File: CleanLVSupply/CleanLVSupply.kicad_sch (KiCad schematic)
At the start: 7 parts, among them J1 12VIN, J2 5V, J3 5V, J4 5V, J5 +-15V, J6 +-15V

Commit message: CleanLVSupply fixes, HiFiDAC skeleton
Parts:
- J5, J6: footprint BW_Connectors:Amphenol_MINITEK_0.8_3P_V -> BW_Connectors:Amphenol_MINITEK_0.8_4P_V; symbol Connector:Conn_01x03_Pin -> Connector:Conn_01x04_Pin
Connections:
- net -15V: now also J5.4 (Pin_4), J6.4 (Pin_4); no longer J5.3 (Pin_3), J6.3 (Pin_3)
- net GND: now also J5.3 (Pin_3), J6.3 (Pin_3)
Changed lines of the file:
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@@
-	)
-	(junction
-		(at 146.05 106.68)
-		(diameter 0)
-		(color 0 0 0 0)
 	)
 	(junction
@@
 	)
 	(junction
+		(at 146.05 109.22)
+		(diameter 0)
+		(color 0 0 0 0)
+	)
+	(junction
+		(at 173.99 90.17)
+		(diameter 0)
+		(color 0 0 0 0)
+	)
+	(junction
 		(at 59.69 110.49)
 		(diameter 0)
@@
 		(color 0 0 0 0)
 	)
+	(junction
+		(at 173.99 104.14)
+		(diameter 0)
+		(color 0 0 0 0)
+	)
 	(wire
 		(pts
@@
 	(wire
 		(pts
-			(xy 176.53 92.71) (xy 146.05 92.71)
-		)
-		(stroke
-			(width 0)
-			(type default)
-		)
-	)
-	(wire
-		(pts
 			(xy 59.69 88.9) (xy 104.14 88.9)
 		)
@@
 	(wire
 		(pts
+			(xy 146.05 109.22) (xy 146.05 95.25)
+		)
+		(stroke
+			(width 0)
+			(type default)
+		)
+	)
+	(wire
+		(pts
 			(xy 87.63 83.82) (xy 87.63 46.99)
 		)
@@
 	(wire
 		(pts
-			(xy 146.05 106.68) (xy 146.05 110.49)
+			(xy 176.53 106.68) (xy 173.99 106.68)
 		)
 		(stroke
@@
 	(wire
 		(pts
+			(xy 173.99 90.17) (xy 176.53 90.17)
+		)
+		(stroke
+			(width 0)
+			(type default)
+		)
+	)
+	(wire
+		(pts
 			(xy 87.63 34.29) (xy 87.63 36.83)
 		)
@@
 	(wire
 		(pts
+			(xy 173.99 104.14) (xy 156.21 104.14)
+		)
+		(stroke
+			(width 0)
+			(type default)
+		)
+	)
+	(wire
+		(pts
 			(xy 68.58 48.26) (xy 68.58 52.07)
 		)
@@
 	(wire
 		(pts
-			(xy 156.21 90.17) (xy 176.53 90.17)
+			(xy 156.21 90.17) (xy 173.99 90.17)
 		)
 		(stroke
@@
 	(wire
 		(pts
+			(xy 146.05 95.25) (xy 176.53 95.25)
+		)
+		(stroke
+			(width 0)
+			(type default)
+		)
+	)
+	(wire
+		(pts
 			(xy 59.69 68.58) (xy 59.69 88.9)
 		)
@@
 	(wire
 		(pts
+			(xy 173.99 92.71) (xy 173.99 90.17)
+		)
+		(stroke
+			(width 0)
+			(type default)
+		)
+	)
+	(wire
+		(pts
 			(xy 166.37 87.63) (xy 176.53 87.63)
 		)
@@
 	(wire
 		(pts
-			(xy 176.53 106.68) (xy 146.05 106.68)
+			(xy 146.05 110.49) (xy 146.05 109.22)
 		)
 		(stroke
@@
 	(wire
 		(pts
+			(xy 146.05 109.22) (xy 176.53 109.22)
+		)
+		(stroke
+			(width 0)
+			(type default)
+		)
+	)
+	(wire
+		(pts
 			(xy 166.37 41.91) (xy 176.53 41.91)
 		)
@@
 	(wire
 		(pts
+			(xy 173.99 106.68) (xy 173.99 104.14)
+		)
+		(stroke
+			(width 0)
+			(type default)
+		)
+	)
+	(wire
+		(pts
 			(xy 156.21 104.14) (xy 156.21 90.17)
 		)
@@
 	(wire
 		(pts
-			(xy 146.05 92.71) (xy 146.05 106.68)
-		)
-		(stroke
-			(width 0)
-			(type default)
-		)
-	)
-	(wire
-		(pts
-			(xy 176.53 104.14) (xy 156.21 104.14)
+			(xy 176.53 104.14) (xy 173.99 104.14)
 		)
 		(stroke
@@
 		(pts
 			(xy 104.14 105.41) (xy 87.63 105.41)
+		)
+		(stroke
+			(width 0)
+			(type default)
+		)
+	)
+	(wire
+		(pts
+			(xy 176.53 92.71) (xy 173.99 92.71)
 		)
 		(stroke
@@
 	)
 	(symbol
-		(lib_id "Connector:Conn_01x03_Pin")
+		(lib_id "Connector:Conn_01x04_Pin")
 		(at 181.61 104.14 0)
 		(mirror y)
@@
 			)
 		)
-		(property "Footprint" "BW_Connectors:Amphenol_MINITEK_0.8_3P_V"
+		(property "Footprint" "BW_Connectors:Amphenol_MINITEK_0.8_4P_V"
 			(at 181.61 104.14 0)
 			(effects
@@
 			)
 		)
-		(property "Description" "Generic connector, single row, 01x03, script generated"
+		(property "Description" "Generic connector, single row, 01x04, script generated"
 			(at 181.61 104.14 0)
 			(effects
@@
 		)
 		(pin "3"
+		)
+		(pin "4"
 		)
 		(instances
@@
 	)
 	(symbol
-		(lib_id "Connector:Conn_01x03_Pin")
+		(lib_id "Connector:Conn_01x04_Pin")
 		(at 181.61 90.17 0)
 		(mirror y)
@@
 			)
 		)
-		(property "Footprint" "BW_Connectors:Amphenol_MINITEK_0.8_3P_V"
+		(property "Footprint" "BW_Connectors:Amphenol_MINITEK_0.8_4P_V"
 			(at 181.61 90.17 0)
 			(effects
@@
 			)
 		)
-		(property "Description" "Generic connector, single row, 01x03, script generated"
+		(property "Description" "Generic connector, single row, 01x04, script generated"
 			(at 181.61 90.17 0)
 			(effects
@@
 		(pin "3"
 		)
+		(pin "4"
+		)
 		(instances

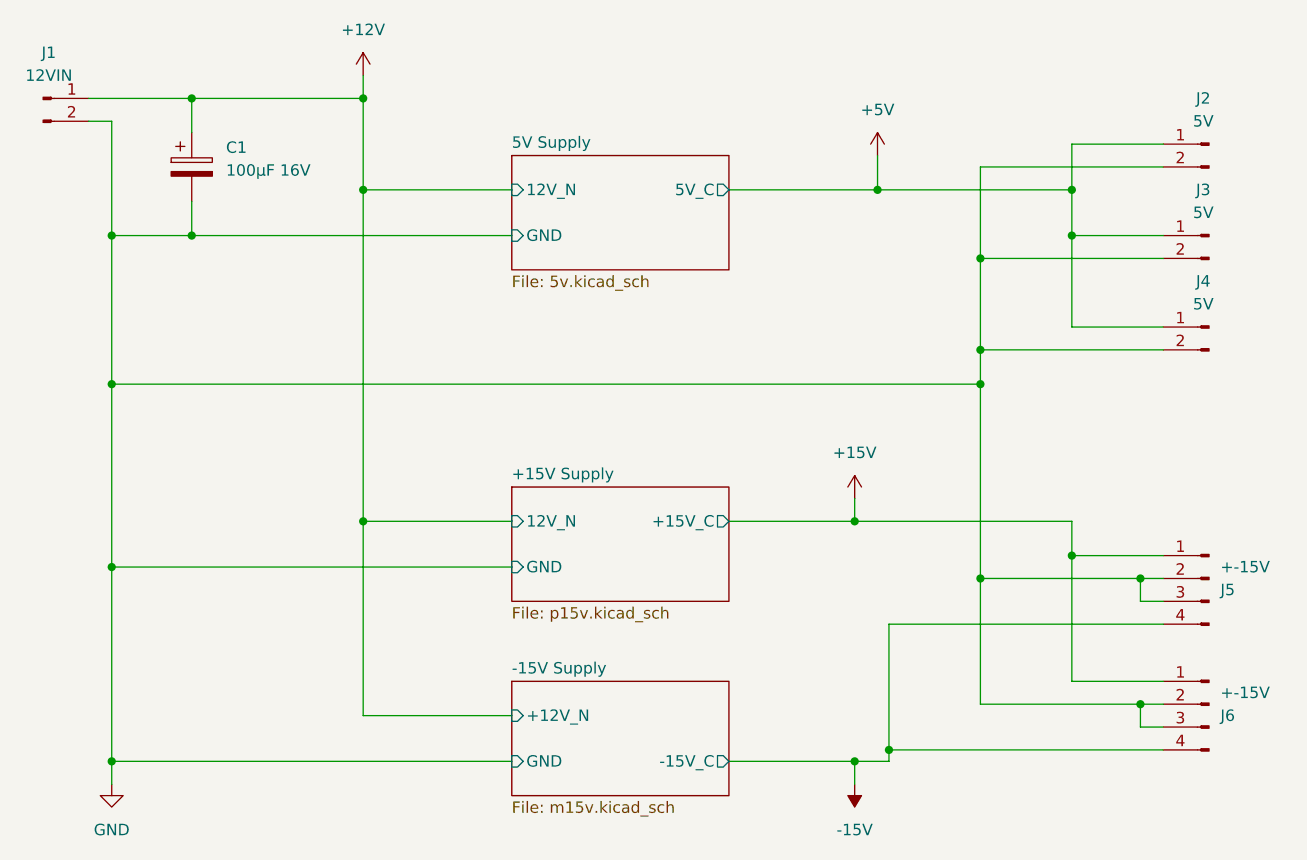
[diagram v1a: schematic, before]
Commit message: HiFiDAC routing done, CleanLVSupply fuses added
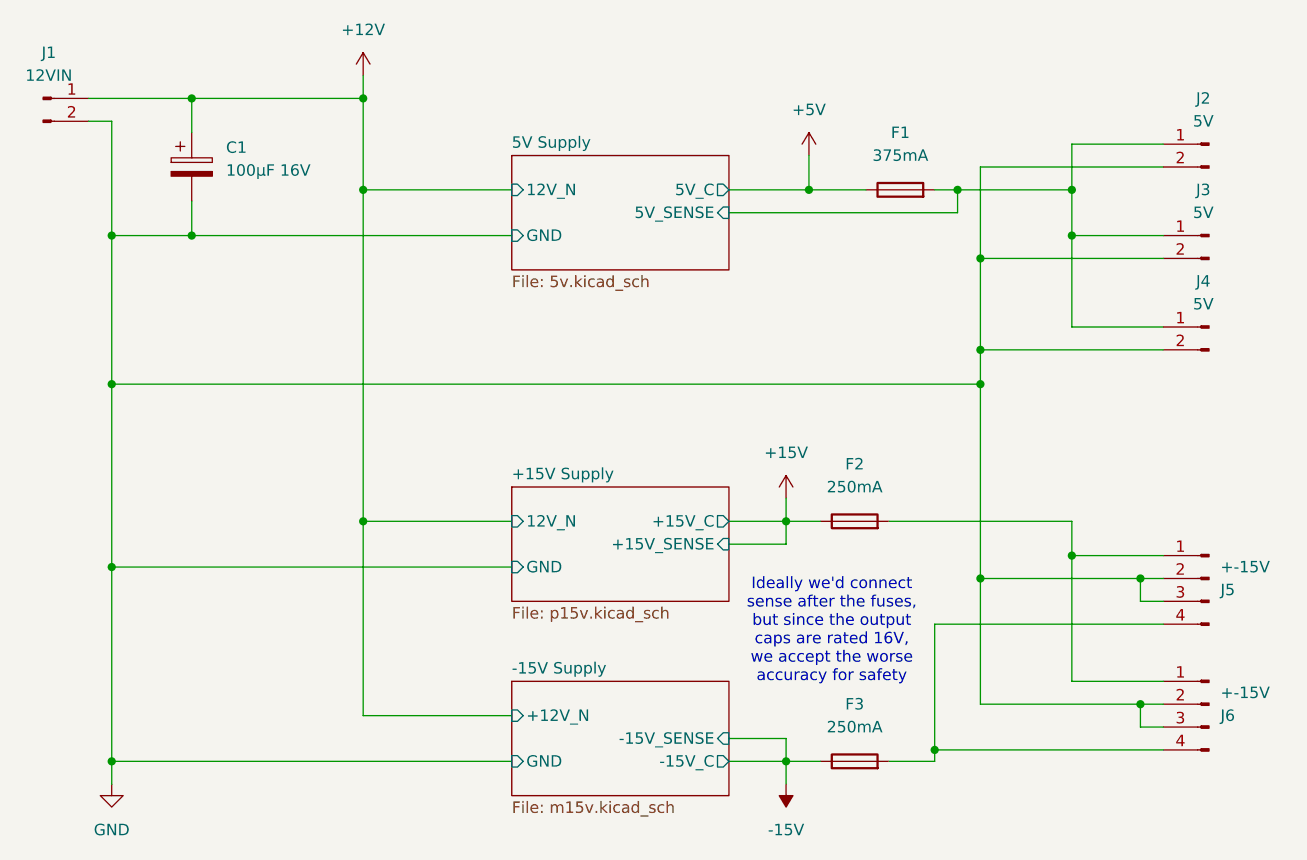
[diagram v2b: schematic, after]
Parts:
- added F1: 375mA, Fuse:Fuse_0603_1608Metric, symbol Device:Fuse
- added F2, F3: 250mA, Fuse:Fuse_0603_1608Metric, symbol Device:Fuse
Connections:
- net +15V: now also F2.1; no longer J5.1 (Pin_1), J6.1 (Pin_1)
- net +5V: now also F1.1; no longer J2.1 (Pin_1), J3.1 (Pin_1), J4.1 (Pin_1)
- net -15V: now also F3.1; no longer J5.4 (Pin_4), J6.4 (Pin_4)
- new net: F2.2, J5.1 (Pin_1), J6.1 (Pin_1)
- new net: F3.2, J5.4 (Pin_4), J6.4 (Pin_4)
- new net 5V Supply/5V_SENSE: F1.2, J2.1 (Pin_1), J3.1 (Pin_1), J4.1 (Pin_1)
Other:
- sheet +15V Supply ports: added +15V_SENSE; removed none
- sheet -15V Supply ports: added -15V_SENSE; removed none
- sheet 5V Supply ports: added 5V_SENSE; removed none
- note added: "Ideally we'd connect sense after the fuses, but since the output caps are rated 16V, we accept the worse accuracy for safety"
